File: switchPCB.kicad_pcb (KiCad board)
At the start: 2 copper layers, 28.5 x 27.8 mm, 6 parts, among them J1 Conn_01x02_Female, J2 Conn_01x02_Female, J3 Conn_01x04_Female, SW1 SW_3PDT_x3

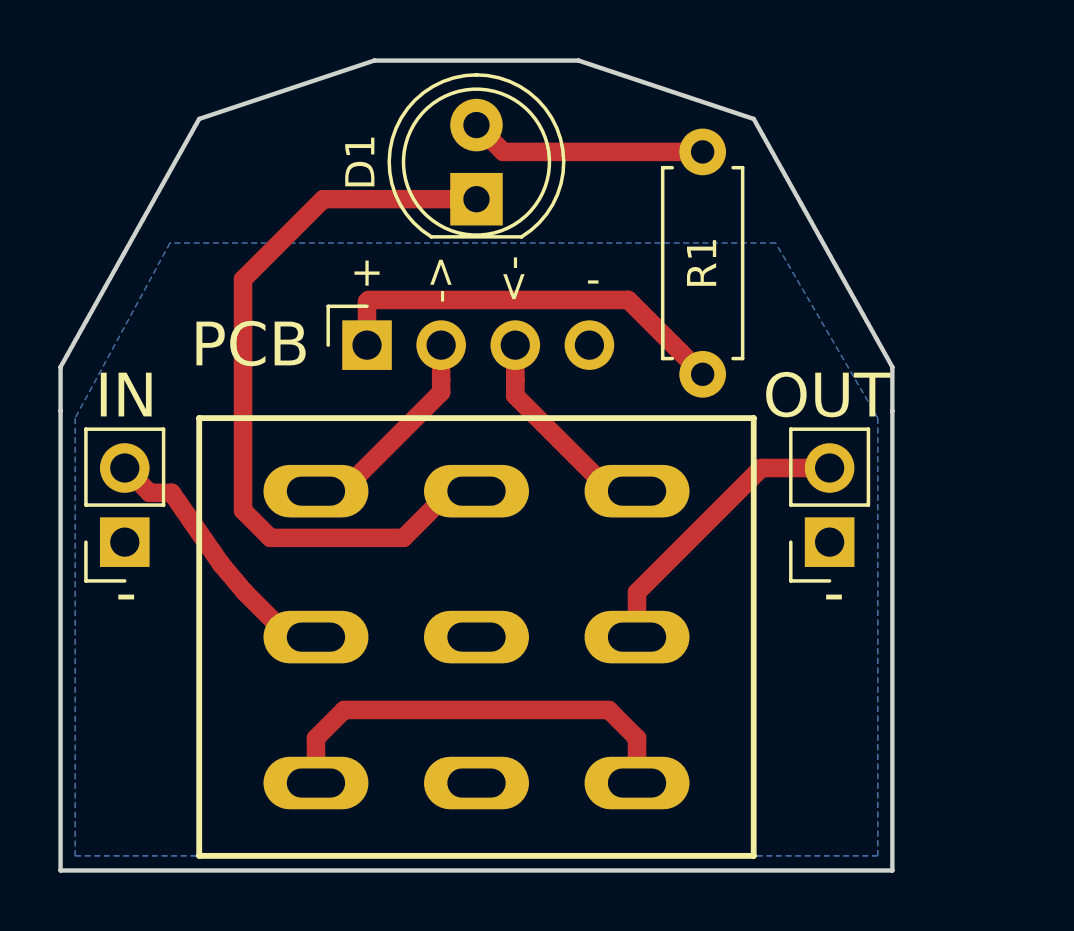
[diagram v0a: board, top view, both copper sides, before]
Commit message: increasing drill hole size on 3pdt sw footprint
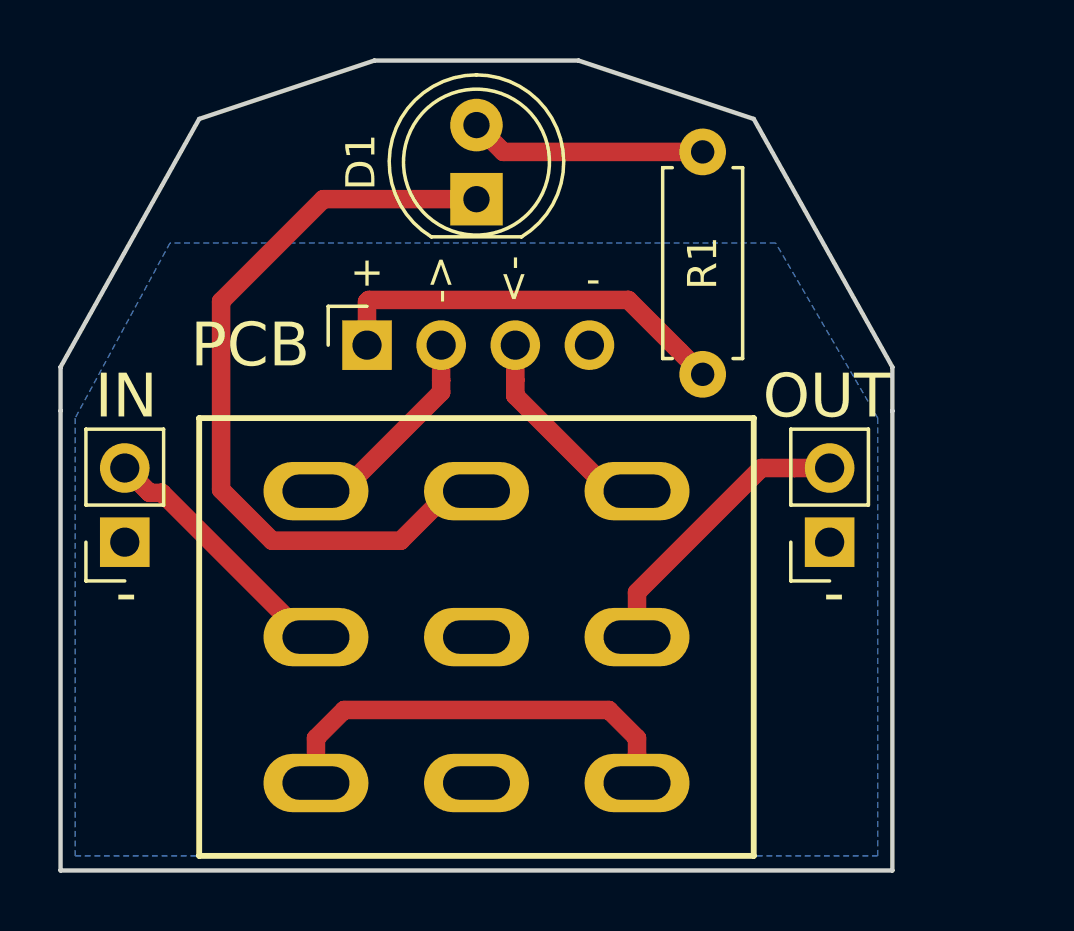
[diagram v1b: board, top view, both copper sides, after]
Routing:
- net Net-(SW1-Pad1): track 14.9 -> 15.9 mm
- net Net-(D1-Pad1): track 26.1 -> 26.8 mm
- net Net-(J3-Pad3): track 7.26 -> 7.97 mm
- net Net-(J3-Pad2): track 7.31 -> 8.02 mm
- net Net-(J1-Pad2): track 9.27 -> 9.85 mm
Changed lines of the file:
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@@
     (thickness 1.6)
     (drawings 25)
-    (tracks 37)
+    (tracks 39)
     (zones 0)
     (modules 6)
@@
     (add_net "Net-(SW1-Pad4)")
   )
+  (module hairyPachyderm:3PDT-footswitch-lugged locked (layer B.Cu)
+    (at 150.7511 112.0036)
+    (fp_text reference SW1 (at 11.5 0) (layer B.SilkS) hide
+      (effects (font (size 1 1) (thickness 0.15)) (justify mirror))
+    )
+    (fp_text value SW_3PDT_x3 (at 0 9) (layer B.Fab)
+      (effects (font (size 1 1) (thickness 0.15)) (justify mirror))
+    )
+    (fp_line (start -9.5 7.5) (end -9.5 0) (layer B.SilkS) (width 0.15))
+    (fp_line (start 9.5 7.5) (end -9.5 7.5) (layer B.SilkS) (width 0.15))
+    (fp_line (start 9.5 -7.5) (end 9.5 7.5) (layer B.SilkS) (width 0.15))
+    (fp_line (start -9.5 -7.5) (end 9.5 -7.5) (layer B.SilkS) (width 0.15))
+    (fp_line (start -9.5 0) (end -9.5 -7.5) (layer B.SilkS) (width 0.15))
+    (fp_circle (center 0 0) (end 0 5.75) (layer B.Fab) (width 0.15))
+    (pad 3 thru_hole oval (at -5.5 -5 90) (size 2 3.6) (drill oval 1.15 2.3) (layers *.Cu *.Mask)
+      (net 7 "Net-(J3-Pad2)"))
+    (pad 6 thru_hole oval (at 0 -5 90) (size 2 3.6) (drill oval 1.15 2.3) (layers *.Cu *.Mask)
+      (net 2 "Net-(D1-Pad1)"))
+    (pad 9 thru_hole oval (at 5.5 -5 90) (size 2 3.6) (drill oval 1.15 2.3) (layers *.Cu *.Mask)
+      (net 8 "Net-(J3-Pad3)"))
+    (pad 2 thru_hole oval (at -5.5 0 90) (size 2 3.6) (drill oval 1.15 2.3) (layers *.Cu *.Mask)
+      (net 4 "Net-(J1-Pad2)"))
+    (pad 5 thru_hole oval (at 0 0 90) (size 2 3.6) (drill oval 1.15 2.3) (layers *.Cu *.Mask)
+      (net 3 GND))
+    (pad 8 thru_hole oval (at 5.5 0 90) (size 2 3.6) (drill oval 1.15 2.3) (layers *.Cu *.Mask)
+      (net 5 "Net-(J2-Pad2)"))
+    (pad 1 thru_hole oval (at -5.5 5 90) (size 2 3.6) (drill oval 1.15 2.3) (layers *.Cu *.Mask)
+      (net 9 "Net-(SW1-Pad1)"))
+    (pad 4 thru_hole oval (at 0 5 90) (size 2 3.6) (drill oval 1.15 2.3) (layers *.Cu *.Mask)
+      (net 10 "Net-(SW1-Pad4)"))
+    (pad 7 thru_hole oval (at 5.5 5 90) (size 2 3.6) (drill oval 1.15 2.3) (layers *.Cu *.Mask)
+      (net 9 "Net-(SW1-Pad1)"))
+  )
   (module Connector_PinSocket_2.54mm:PinSocket_1x04_P2.54mm_Vertical (layer F.Cu)
     (at 150.75 102 90)
@@
     )
   )
-  (module hairyPachyderm:3PDT-footswitch-lugged locked (layer B.Cu)
-    (at 150.7511 112.0036)
-    (fp_text reference SW1 (at 11.5 0) (layer B.SilkS) hide
-      (effects (font (size 1 1) (thickness 0.15)) (justify mirror))
-    )
-    (fp_text value SW_3PDT_x3 (at 0 9) (layer B.Fab)
-      (effects (font (size 1 1) (thickness 0.15)) (justify mirror))
-    )
-    (fp_line (start -9.5 7.5) (end -9.5 0) (layer B.SilkS) (width 0.15))
-    (fp_line (start 9.5 7.5) (end -9.5 7.5) (layer B.SilkS) (width 0.15))
-    (fp_line (start 9.5 -7.5) (end 9.5 7.5) (layer B.SilkS) (width 0.15))
-    (fp_line (start -9.5 -7.5) (end 9.5 -7.5) (layer B.SilkS) (width 0.15))
-    (fp_line (start -9.5 0) (end -9.5 -7.5) (layer B.SilkS) (width 0.15))
-    (fp_circle (center 0 0) (end 0 5.75) (layer B.Fab) (width 0.15))
-    (pad 3 thru_hole oval (at -5.5 -5 90) (size 1.8 3.6) (drill oval 1 2) (layers *.Cu *.Mask)
-      (net 7 "Net-(J3-Pad2)"))
-    (pad 6 thru_hole oval (at 0 -5 90) (size 1.8 3.6) (drill oval 1 2) (layers *.Cu *.Mask)
-      (net 2 "Net-(D1-Pad1)"))
-    (pad 9 thru_hole oval (at 5.5 -5 90) (size 1.8 3.6) (drill oval 1 2) (layers *.Cu *.Mask)
-      (net 8 "Net-(J3-Pad3)"))
-    (pad 2 thru_hole oval (at -5.5 0 90) (size 1.8 3.6) (drill oval 1 2) (layers *.Cu *.Mask)
-      (net 4 "Net-(J1-Pad2)"))
-    (pad 5 thru_hole oval (at 0 0 90) (size 1.8 3.6) (drill oval 1 2) (layers *.Cu *.Mask)
-      (net 3 GND))
-    (pad 8 thru_hole oval (at 5.5 0 90) (size 1.8 3.6) (drill oval 1 2) (layers *.Cu *.Mask)
-      (net 5 "Net-(J2-Pad2)"))
-    (pad 1 thru_hole oval (at -5.5 5 90) (size 1.8 3.6) (drill oval 1 2) (layers *.Cu *.Mask)
-      (net 9 "Net-(SW1-Pad1)"))
-    (pad 4 thru_hole oval (at 0 5 90) (size 1.8 3.6) (drill oval 1 2) (layers *.Cu *.Mask)
-      (net 10 "Net-(SW1-Pad4)"))
-    (pad 7 thru_hole oval (at 5.5 5 90) (size 1.8 3.6) (drill oval 1 2) (layers *.Cu *.Mask)
-      (net 9 "Net-(SW1-Pad1)"))
-  )
   (gr_text - (at 163 110.5) (layer F.SilkS)
     (effects (font (size 1.5 1.5) (thickness 0.3)))
@@
   (segment (start 151.67 95.38) (end 150.75 94.46) (width 0.635) (layer F.Cu) (net 1))
   (segment (start 158.5 95.38) (end 151.67 95.38) (width 0.635) (layer F.Cu) (net 1))
-  (segment (start 148.25259 108.60211) (end 143.688976 108.60211) (width 0.635) (layer F.Cu) (net 2))
-  (segment (start 149.8511 107.0036) (end 148.25259 108.60211) (width 0.635) (layer F.Cu) (net 2))
-  (segment (start 142.75259 107.665724) (end 142.75259 99.74741) (width 0.635) (layer F.Cu) (net 2))
-  (segment (start 143.688976 108.60211) (end 142.75259 107.665724) (width 0.635) (layer F.Cu) (net 2))
+  (segment (start 142 100.5) (end 145.5 97) (width 0.635) (layer F.Cu) (net 2))
+  (segment (start 149.8511 107.0036) (end 148.15259 108.70211) (width 0.635) (layer F.Cu) (net 2))
+  (segment (start 145.5 97) (end 150.75 97) (width 0.635) (layer F.Cu) (net 2))
   (segment (start 150.7511 107.0036) (end 149.8511 107.0036) (width 0.635) (layer F.Cu) (net 2))
-  (segment (start 145.5 97) (end 150.75 97) (width 0.635) (layer F.Cu) (net 2))
-  (segment (start 142.75259 99.74741) (end 145.5 97) (width 0.635) (layer F.Cu) (net 2))
+  (segment (start 148.15259 108.70211) (end 143.747555 108.70211) (width 0.635) (layer F.Cu) (net 2))
+  (segment (start 143.747555 108.70211) (end 142 106.954555) (width 0.635) (layer F.Cu) (net 2))
+  (segment (start 142 106.954555) (end 142 100.5) (width 0.635) (layer F.Cu) (net 2))
+  (segment (start 145.2511 112.0036) (end 144.3511 112.0036) (width 0.635) (layer F.Cu) (net 4))
   (segment (start 139.549999 107.059999) (end 138.7 106.21) (width 0.635) (layer F.Cu) (net 4))
-  (segment (start 144.3511 112.0036) (end 142.8161 110.4686) (width 0.635) (layer F.Cu) (net 4))
-  (segment (start 145.2511 112.0036) (end 144.3511 112.0036) (width 0.635) (layer F.Cu) (net 4))
-  (segment (start 142.8161 110.4686) (end 142 109.5) (width 0.635) (layer F.Cu) (net 4))
-  (segment (start 142 109.5) (end 140.307499 107.059999) (width 0.635) (layer F.Cu) (net 4))
-  (segment (start 140.307499 107.059999) (end 139.549999 107.059999) (width 0.635) (layer F.Cu) (net 4))
+  (segment (start 139.967301 107.059999) (end 139.549999 107.059999) (width 0.635) (layer F.Cu) (net 4))
+  (segment (start 144.910902 112.0036) (end 139.967301 107.059999) (width 0.635) (layer F.Cu) (net 4))
+  (segment (start 145.2511 112.0036) (end 144.910902 112.0036) (width 0.635) (layer F.Cu) (net 4))
   (segment (start 160.5097 106.21) (end 161.647919 106.21) (width 0.635) (layer F.Cu) (net 5))
   (segment (start 156.2511 110.4686) (end 160.5097 106.21) (width 0.635) (layer F.Cu) (net 5))
@@
   (segment (start 149.54 103.6147) (end 149.54 103.202081) (width 0.635) (layer F.Cu) (net 7))
   (segment (start 146.1511 107.0036) (end 149.54 103.6147) (width 0.635) (layer F.Cu) (net 7))
+  (segment (start 146.1511 107.0036) (end 146.6547 106.5) (width 0.635) (layer F.Cu) (net 7))
   (segment (start 145.2511 107.0036) (end 146.1511 107.0036) (width 0.635) (layer F.Cu) (net 7))
   (segment (start 152.08 103.202081) (end 152.08 102) (width 0.635) (layer F.Cu) (net 8))
   (segment (start 152.08 103.7325) (end 152.08 103.202081) (width 0.635) (layer F.Cu) (net 8))
   (segment (start 155.3511 107.0036) (end 152.08 103.7325) (width 0.635) (layer F.Cu) (net 8))
+  (segment (start 155.3511 107.0036) (end 154.8475 106.5) (width 0.635) (layer F.Cu) (net 8))
   (segment (start 156.2511 107.0036) (end 155.3511 107.0036) (width 0.635) (layer F.Cu) (net 8))
   (segment (start 156.2511 115.4686) (end 156.2511 117.0036) (width 0.635) (layer F.Cu) (net 9))
-  (segment (start 146.2197 114.5) (end 155.2825 114.5) (width 0.635) (layer F.Cu) (net 9))
   (segment (start 155.2825 114.5) (end 156.2511 115.4686) (width 0.635) (layer F.Cu) (net 9))
   (segment (start 145.2511 115.4686) (end 146.2197 114.5) (width 0.635) (layer F.Cu) (net 9))
+  (segment (start 146.2197 114.5) (end 155.2825 114.5) (width 0.635) (layer F.Cu) (net 9))
   (segment (start 145.2511 117.0036) (end 145.2511 115.4686) (width 0.635) (layer F.Cu) (net 9))
+  (segment (start 156.2511 117.0036) (end 156.2511 116) (width 0.635) (layer F.Cu) (net 9))
   (zone (net 3) (net_name GND) (layer B.Cu) (hatch edge 0.508)
     (connect_pads (clearance 0.508))

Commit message: LED on the out side
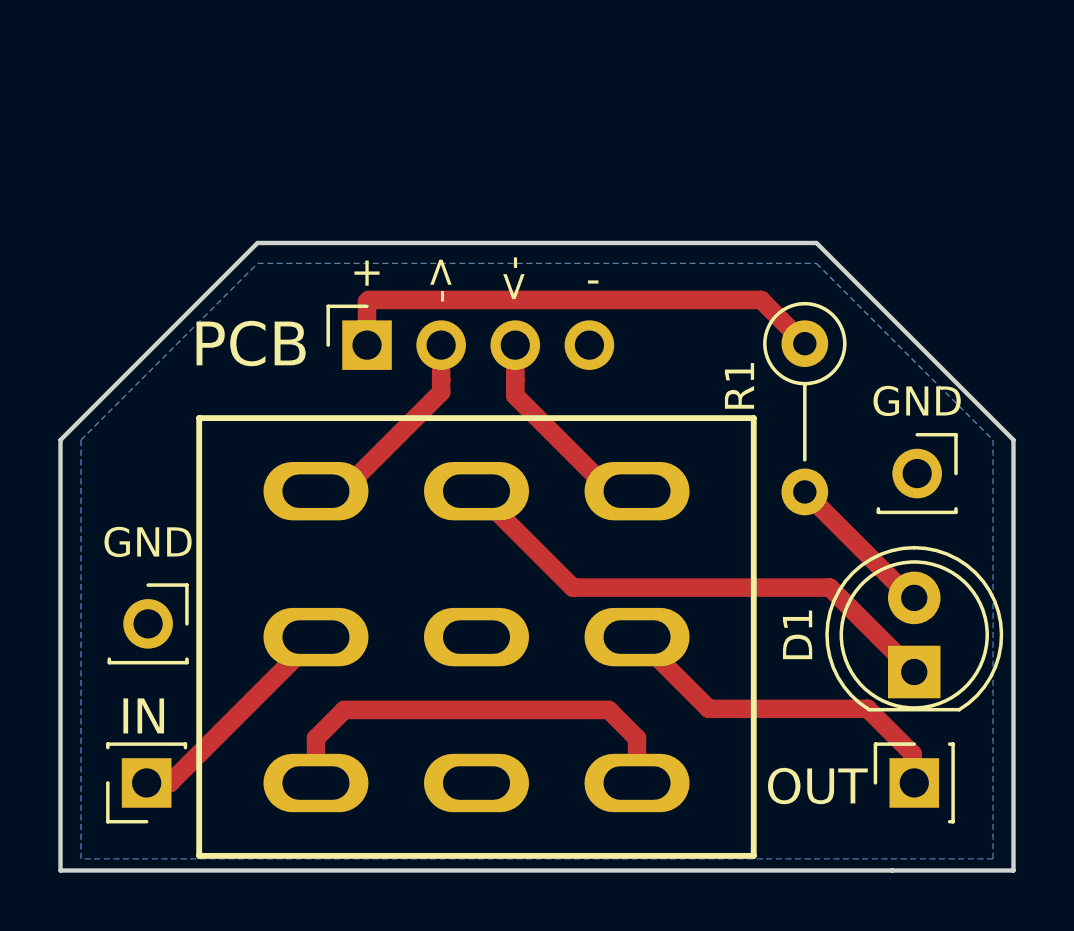
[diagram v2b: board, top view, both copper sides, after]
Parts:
- added GND: PinSocket_1x01_P2.54mm_Vertical, Connector_PinSocket_2.54mm:PinSocket_1x01_P2.54mm_Vertical, F.Cu at (139.5, 111.5)
- added GND: PinSocket_1x01_P2.54mm_Vertical, Connector_PinSocket_2.54mm:PinSocket_1x01_P2.54mm_Vertical, F.Cu at (165.8, 106.4)
- J1, J2: footprint Connector_PinSocket_2.54mm:PinSocket_1x02_P2.54mm_Vertical -> Connector_PinSocket_2.54mm:PinSocket_1x01_P2.54mm_Vertical
- R1: footprint Resistor_THT:R_Axial_DIN0207_L6.3mm_D2.5mm_P7.62mm_Horizontal -> Resistor_THT:R_Axial_DIN0207_L6.3mm_D2.5mm_P5.08mm_Vertical
- moved D1 22.1 mm to (165.8, 113.2)
- moved J2 8.74 mm to (165.8, 117.0), turned to 90 degrees
- moved J1 8.28 mm to (139.4, 117.0)
- moved R1 3.65 mm to (162.0, 102.0), turned to 270 degrees
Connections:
- J1 pad 1: GND -> Net-(J1-Pad1)
- J2 pad 1: GND -> Net-(J2-Pad1)
- SW1 pad 2: Net-(J1-Pad2) -> Net-(J1-Pad1)
- SW1 pad 4: Net-(SW1-Pad4) -> (no net)
- SW1 pad 8: Net-(J2-Pad2) -> Net-(J2-Pad1)
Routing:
- net Net-(J2-Pad1): track 0.00 -> 12.3 mm
- net Net-(J2-Pad2): track 9.90 -> 0.00 mm
- net Net-(J1-Pad2): track 9.85 -> 0.00 mm
- net Net-(D1-Pad1): track 26.8 -> 17.6 mm
- net Net-(J1-Pad1): track 0.00 -> 8.77 mm
- net Net-(J3-Pad1): track 14.1 -> 17.1 mm
- net Net-(D1-Pad2): track 8.13 -> 5.63 mm
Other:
- board size 28.5 x 27.8 mm -> 32.7 x 21.5 mm
- board text removed: "BYPASS LED HERE"
